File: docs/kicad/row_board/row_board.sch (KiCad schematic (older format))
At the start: 19 parts, among them J1 Conn_01x06, J2 Conn_01x06, SW1 SW1, SW2 SW1, SW3 SW1, SW4 SW1, SW5 SW1, U1 74HC595

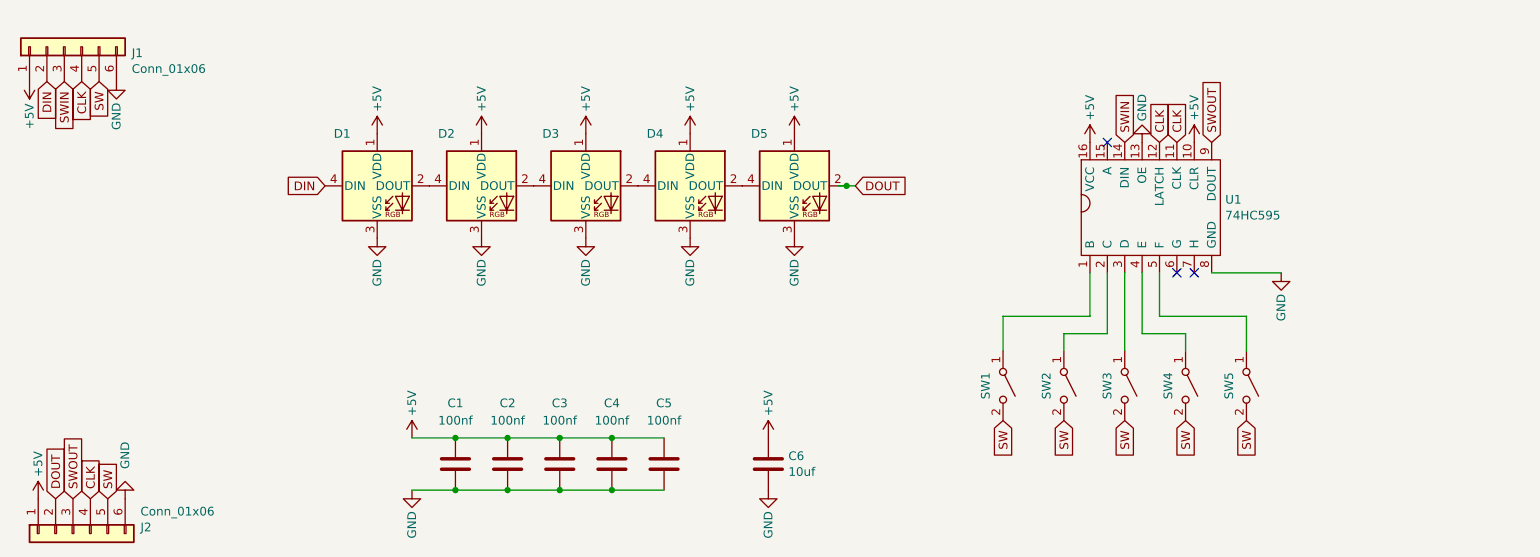
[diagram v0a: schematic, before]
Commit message: got rid of (many) vestigial TE3 design attempts; consolidating electronics under TE3/docs/kicad
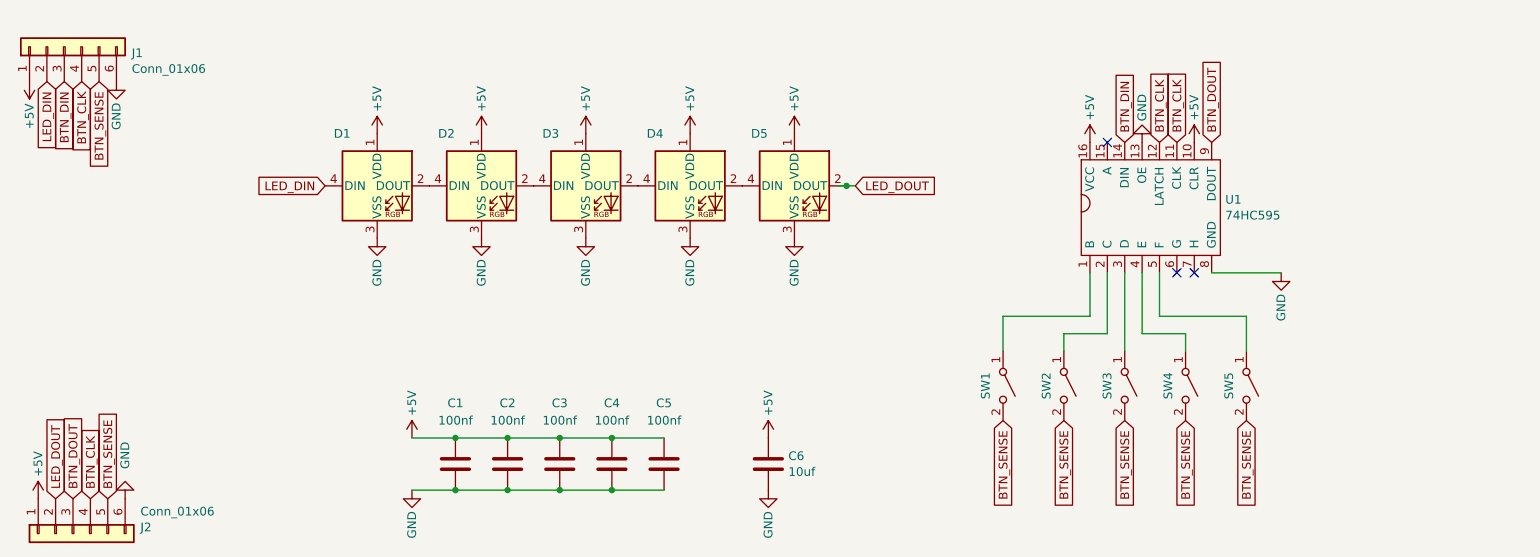
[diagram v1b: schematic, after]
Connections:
- net labels added: BTN_CLK, BTN_DIN, BTN_DOUT, BTN_SENSE, LED_DIN, LED_DOUT
- net labels removed: CLK, DIN, DOUT, SW, SWIN, SWOUT
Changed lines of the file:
@@
 $EndComp
 Text GLabel 850  1000 3    50   Input ~ 0
-DIN
+LED_DIN
 $Comp
 L Connector_Generic:Conn_01x06 J1
@@
 $EndComp
 Text GLabel 1050 1000 3    50   Input ~ 0
-CLK
+BTN_CLK
 Text GLabel 950  1000 3    50   Input ~ 0
-SWIN
-Text GLabel 1150 1000 3    50   Input ~ 0
-SW
+BTN_DIN
 Text GLabel 900  3400 1    50   Input ~ 0
-DOUT
-Text GLabel 1100 3400 1    50   Input ~ 0
-CLK
+LED_DOUT
 Text GLabel 1000 3400 1    50   Input ~ 0
-SWOUT
-Text GLabel 1200 3400 1    50   Input ~ 0
-SW
+BTN_DOUT
 $Comp
 L Switch:SW_SPST SW2
@@
 $EndComp
 Text GLabel 6350 2950 3    50   Input ~ 0
-SW
-Text GLabel 6700 2950 3    50   Input ~ 0
-SW
-Text GLabel 7050 2950 3    50   Input ~ 0
-SW
-Text GLabel 7400 2950 3    50   Input ~ 0
-SW
-Text GLabel 7750 2950 3    50   Input ~ 0
-SW
+BTN_SENSE
 Wire Wire Line
 	7050 2550 7050 2100
@@
 $EndComp
 Text GLabel 7050 1350 1    50   Input ~ 0
-SWIN
+BTN_DIN
 Text GLabel 7550 1350 1    50   Input ~ 0
-SWOUT
+BTN_DOUT
 Text GLabel 7350 1350 1    50   Input ~ 0
-CLK
+BTN_CLK
 NoConn ~ 7350 2100
 NoConn ~ 7450 2100
@@
 $EndComp
 Text GLabel 7250 1350 1    50   Input ~ 0
-CLK
+BTN_CLK
 $Comp
 L power:+5V #PWR07
@@
 	5400 1600 5450 1600
 Text GLabel 5500 1600 2    50   Input ~ 0
-DOUT
+LED_DOUT
 Text GLabel 2450 1600 0    50   Input ~ 0
-DIN
+LED_DIN
 $Comp
 L LED:WS2812B D2
@@
 Wire Wire Line
 	4100 3350 4400 3350
+Text GLabel 1100 3400 1    50   Input ~ 0
+BTN_CLK
+Text GLabel 6700 2950 3    50   Input ~ 0
+BTN_SENSE
+Text GLabel 7050 2950 3    50   Input ~ 0
+BTN_SENSE
+Text GLabel 7400 2950 3    50   Input ~ 0
+BTN_SENSE
+Text GLabel 7750 2950 3    50   Input ~ 0
+BTN_SENSE
+Text GLabel 1150 1000 3    50   Input ~ 0
+BTN_SENSE
+Text GLabel 1200 3400 1    50   Input ~ 0
+BTN_SENSE
 $EndSCHEMATC

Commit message: initial kicad design of TE3 mother_board
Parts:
- added R?: 100, symbol Device:R
- added R?: 220, symbol Device:R
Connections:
- wire segments 26 -> 28
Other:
- note added: "Note that supply voltage is \ndivided down to 3.3V for\ncompatibility with teensy4.1"
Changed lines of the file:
@@
 L power:+5V #PWR03
 U 1 1 660AD766
-P 6850 1350
-F 0 "#PWR03" H 6850 1200 50  0001 C CNN
-F 1 "+5V" V 6850 1550 50  0000 C CNN
-F 2 "" H 6850 1350 50  0001 C CNN
-F 3 "" H 6850 1350 50  0001 C CNN
-	1    6850 1350
+P 6850 1050
+F 0 "#PWR03" H 6850 900 50  0001 C CNN
+F 1 "+5V" V 6850 1250 50  0000 C CNN
+F 2 "" H 6850 1050 50  0001 C CNN
+F 3 "" H 6850 1050 50  0001 C CNN
+	1    6850 1050
 	1    0    0    -1
 $EndComp
@@
 Text GLabel 1200 3400 1    50   Input ~ 0
 BTN_SENSE
+$Comp
+L Device:R R?
+U 1 1 67948ED1
+P 6850 1200
+F 0 "R?" H 6650 1250 50  0000 L CNN
+F 1 "100" V 6850 1200 50  0000 C CNN
+F 2 "" V 6780 1200 50  0001 C CNN
+F 3 "~" H 6850 1200 50  0001 C CNN
+	1    6850 1200
+	1    0    0    -1
+$EndComp
+$Comp
+L Device:R R?
+U 1 1 6794FF15
+P 6550 1550
+F 0 "R?" H 6350 1600 50  0000 L CNN
+F 1 "220" V 6550 1550 50  0000 C CNN
+F 2 "" V 6480 1550 50  0001 C CNN
+F 3 "~" H 6550 1550 50  0001 C CNN
+	1    6550 1550
+	1    0    0    -1
+$EndComp
+Wire Wire Line
+	6850 1350 6550 1350
+Wire Wire Line
+	6550 1350 6550 1400
+Connection ~ 6850 1350
+$Comp
+L power:GND #PWR?
+U 1 1 67952185
+P 6550 1700
+F 0 "#PWR?" H 6550 1450 50  0001 C CNN
+F 1 "GND" V 6550 1500 50  0000 C CNN
+F 2 "" H 6550 1700 50  0001 C CNN
+F 3 "" H 6550 1700 50  0001 C CNN
+	1    6550 1700
+	1    0    0    -1
+$EndComp
+Text Notes 8000 1350 0    50   ~ 0
+Note that supply voltage is \ndivided down to 3.3V for\ncompatibility with teensy4.1
 $EndSCHEMATC
